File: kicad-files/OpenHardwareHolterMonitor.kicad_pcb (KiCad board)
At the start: 8 copper layers, 131 x 80 mm, 147 parts, among them CON1 Micro_SD_Card, J1 Conn_02x06_Odd_Even, J10 Conn_01x01, J11 Conn_01x01, J12 USB_OTG, J13 USB_C_Receptacle, J2 Conn_01x01, J3 Conn_01x01, J4 Conn_01x01, J5 Conn_01x01, J6 Conn_01x01, J7 Conn_01x01, J8 Conn_01x01, J9 Conn_01x01, P1 Custom_FTDI, Q1 S8050, Q10 Q_PMOS_DGS, Q2 S8050, Q3 Q_NMOS_DGS, Q4 Q_NMOS_DGS, Q5 Q_NMOS_DGS, Q6 Q_NMOS_DGS, Q7 Q_PMOS_DGS, Q8 Q_PMOS_DGS, Q9 Q_PMOS_DGS, SW1 SW_SPDT, U1 ESP-WROOM-32, U2 ADS1298, U3 MCP73833, U4 MCP73833, U5 TPS2113A, U6 LP5912, U7 REM_3-xxxxS, Y1 32768Hz

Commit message: checkpoint for kicad upgrade
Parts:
- added MH_NE: MountingHole_2.2mm_M2_ISO7380, Mounting_Holes:MountingHole_2.2mm_M2_ISO7380, F.Cu at (258.0, 28.0)
- added MH_NW: MountingHole_2.2mm_M2_ISO7380, Mounting_Holes:MountingHole_2.2mm_M2_ISO7380, F.Cu at (145.5, 43.5)
- added MH_SE: MountingHole_2.2mm_M2_ISO7380, Mounting_Holes:MountingHole_2.2mm_M2_ISO7380, F.Cu at (258.0, 92.0)
- added MH_SW: MountingHole_2.2mm_M2_ISO7380, Mounting_Holes:MountingHole_2.2mm_M2_ISO7380, F.Cu at (161.5, 84.0)
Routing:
- net /IO0: track 49.0 -> 46.0 mm
- net /EN: track 52.0 -> 51.3 mm
- net /RTS: track 33.9 -> 33.1 mm
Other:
- board text added: "EU: N (black)"
- board text added: "US: RL (green)"

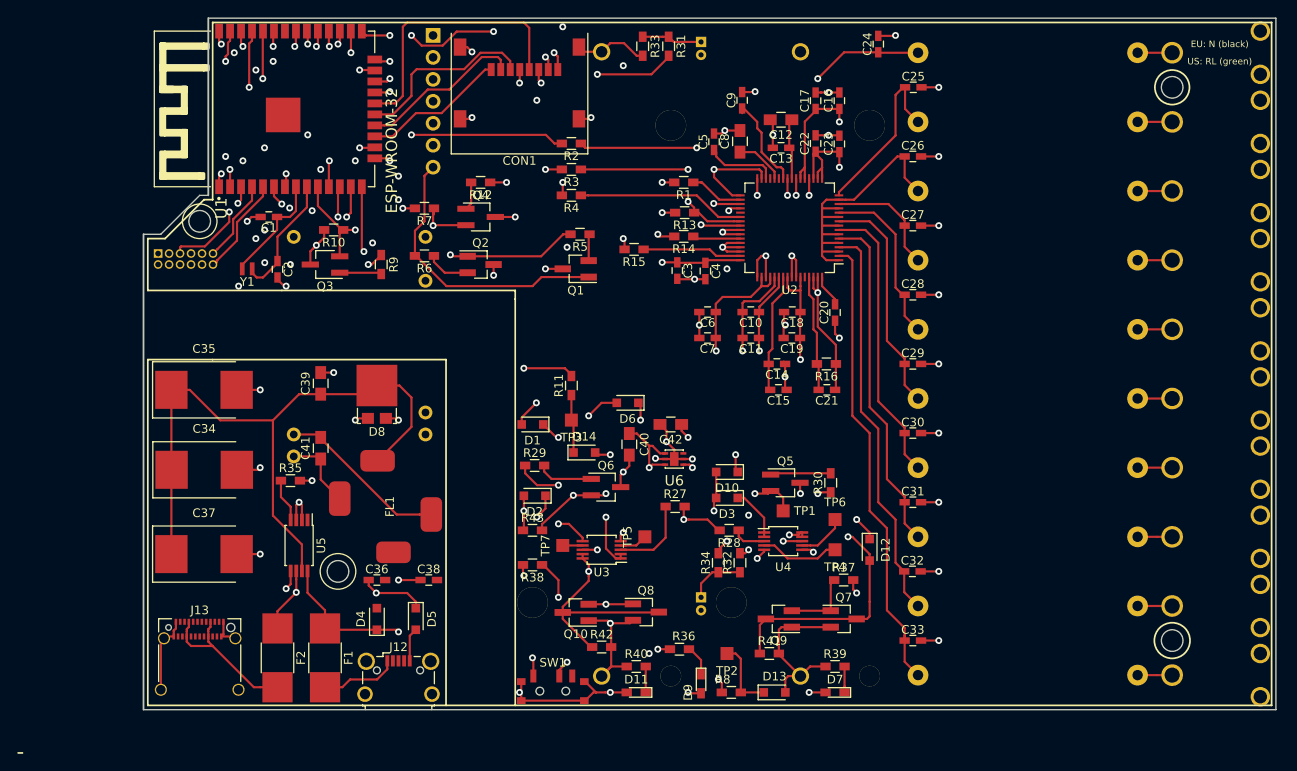
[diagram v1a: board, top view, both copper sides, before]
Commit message: switch to 6 layer board
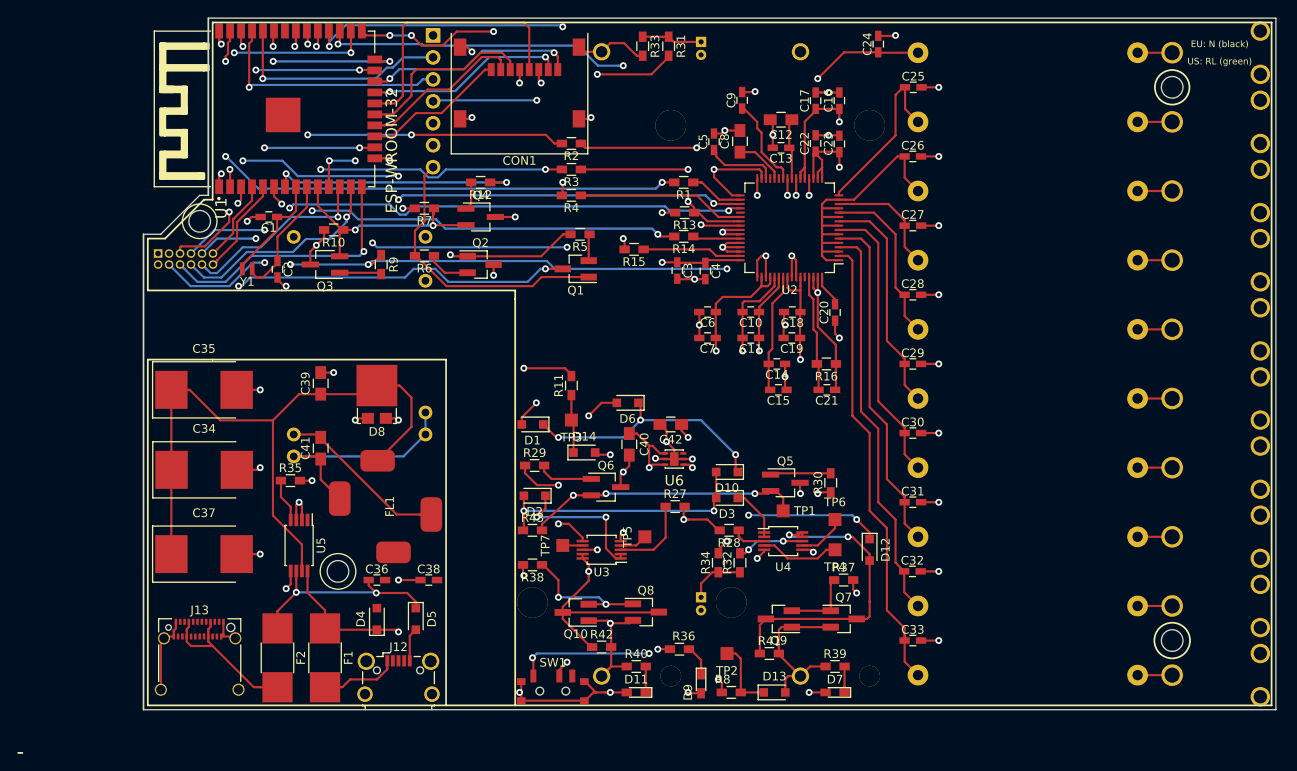
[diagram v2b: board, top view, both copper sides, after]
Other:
- copper layers 8 -> 6

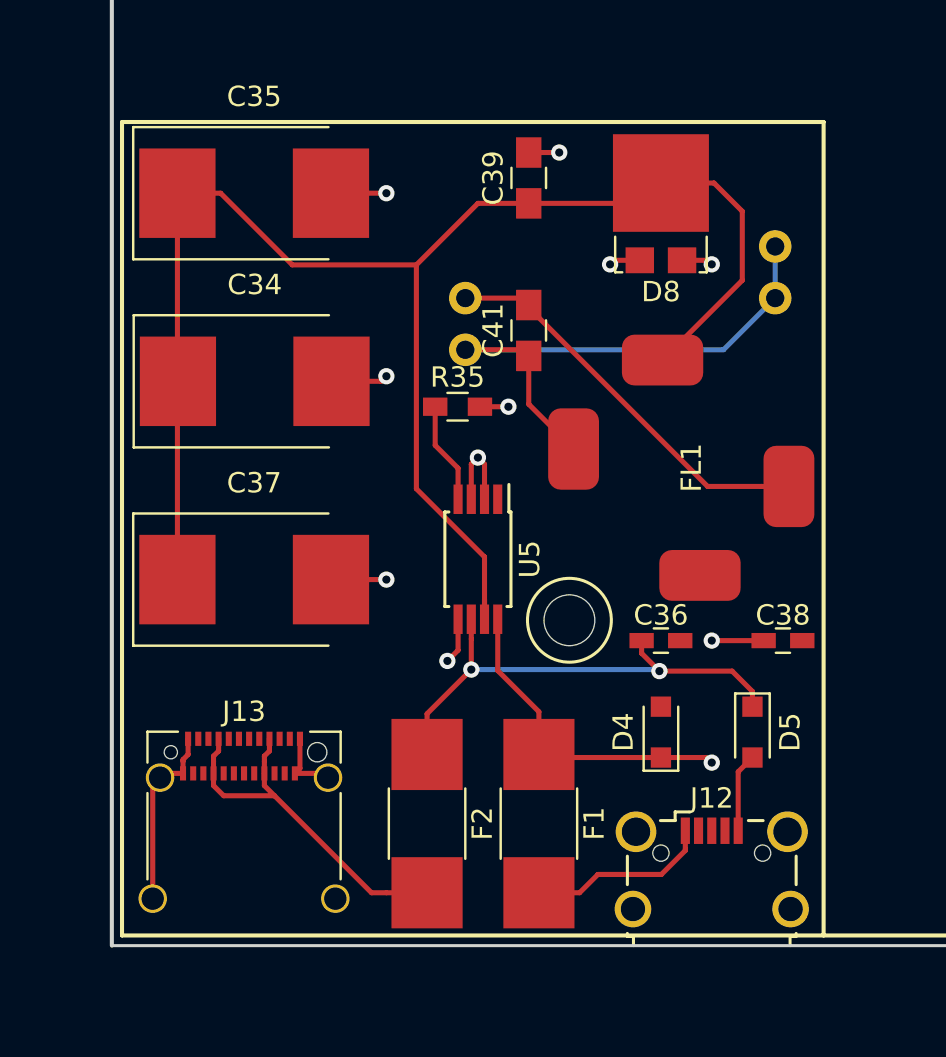
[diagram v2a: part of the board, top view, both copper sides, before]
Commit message: power lines 0.5mm
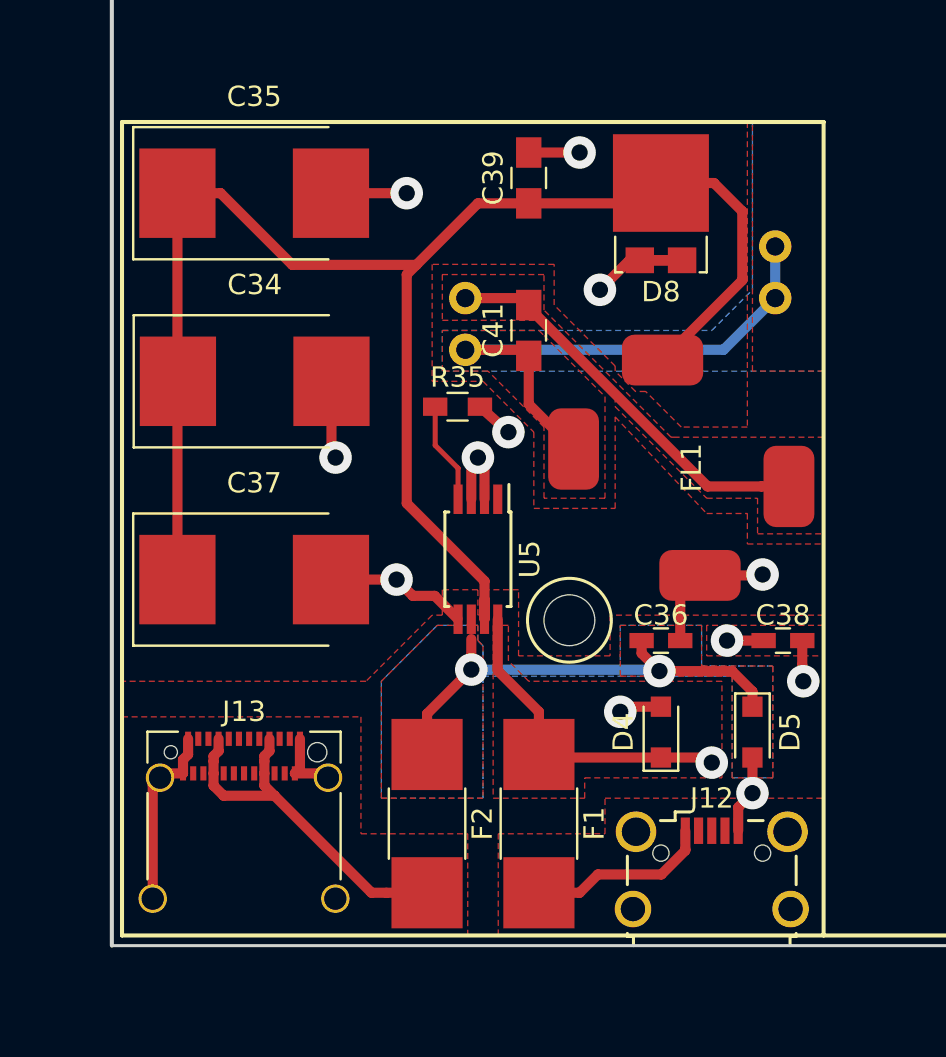
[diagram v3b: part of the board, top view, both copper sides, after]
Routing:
- net GNDPWR: track 37.4 -> 57.4 mm, vias 9 -> 11
- net /power/USB_C_IN: track 24.4 -> 23.5 mm
- added copper zone on In2.Cu.power, net (none)
- added copper zone on F.Cu, net +5C
- added copper zone on In2.Cu.power, net +5C
- added copper zone on F.Cu, net +5V
- added copper zone on F.Cu, net /power/MUX_POWER_OUT
- added copper zone on In2.Cu.power, net /power/MUX_POWER_OUT
- added copper zone on B.Cu, net /power/USB_C_IN
- added copper zone on F.Cu, net /power/USB_C_IN
- added copper zone on F.Cu, net /power/USB_MICRO_IN
- added copper zone on In3.Cu.vert, net /power/USB_MICRO_IN
- added copper zone on In1.Cu.gnd, net GNDPWR
- added copper zone on In4.Cu.gnd, net GNDPWR
- added copper zone on B.Cu, net Net-(C41-Pad1)
- added copper zone on F.Cu, net Net-(C41-Pad1)
- added copper zone on F.Cu, net Net-(C41-Pad2)
- added copper zone on In2.Cu.power, net Net-(C41-Pad2)
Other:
- net class Power added: clearance 0.2, trace_width 0.5, via_dia 1.6, via_drill 0.8

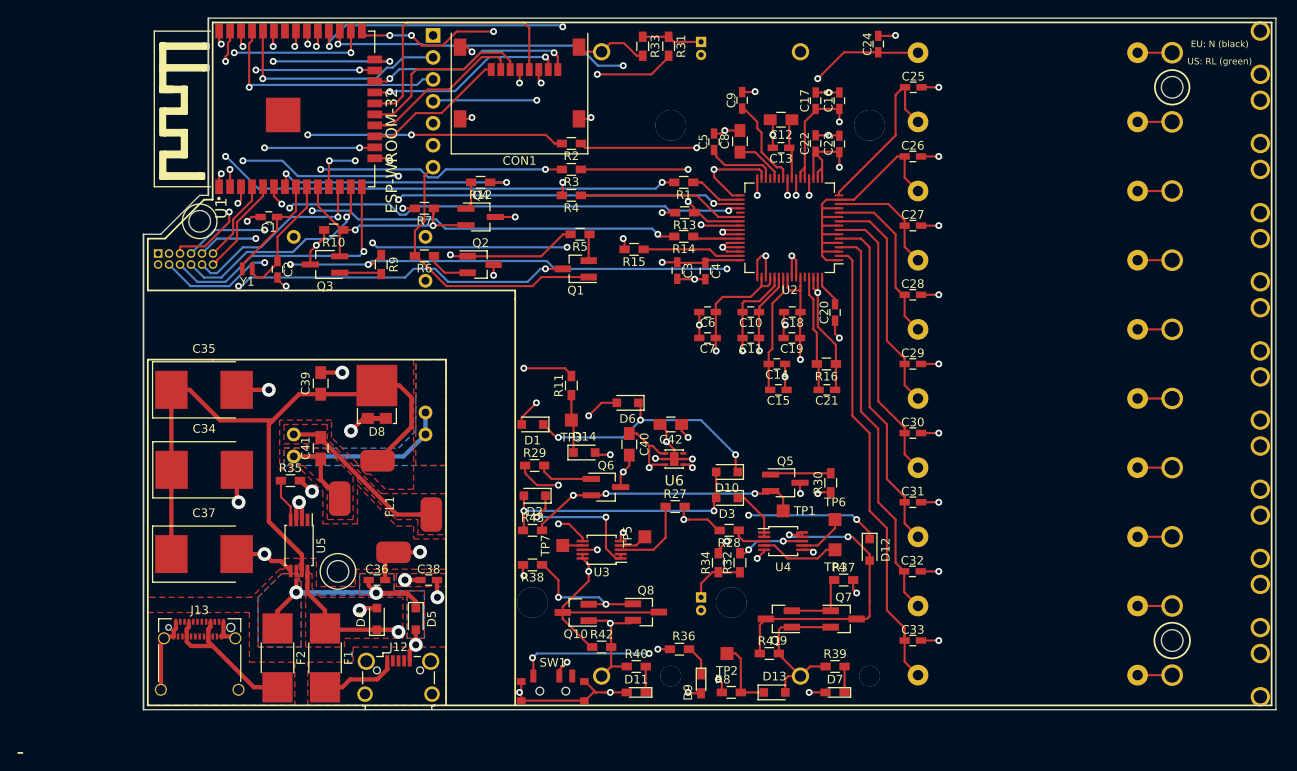
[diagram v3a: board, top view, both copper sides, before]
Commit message: isolated ground planes
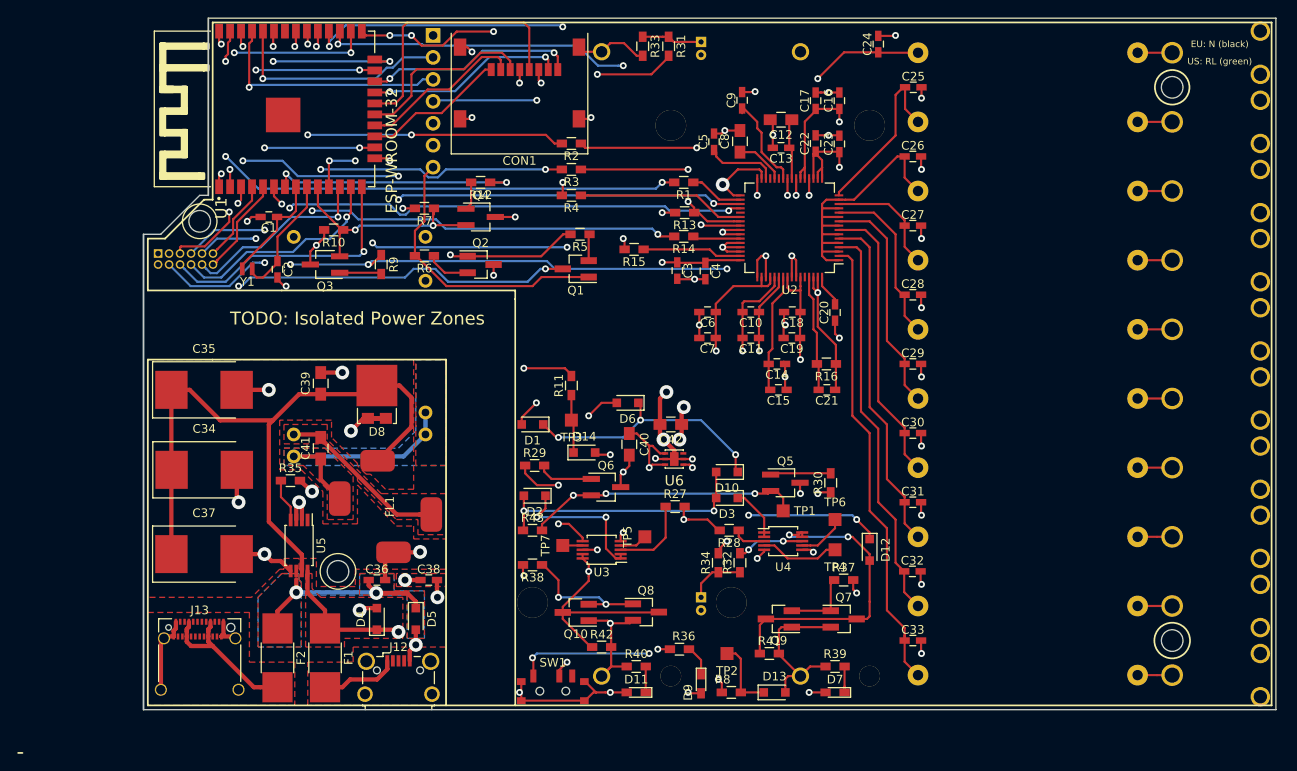
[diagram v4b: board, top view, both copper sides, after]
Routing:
- net GND: track 174.0 -> 170.5 mm, vias 56 -> 57
- net +3V3: track 109.3 -> 112.2 mm, vias 13 -> 14
- added copper zone on In2.Cu.power, net +3V3
- added copper zone on In1.Cu.gnd, net GND
- added copper zone on In4.Cu.gnd, net GND
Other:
- board text added: "TODO: Isolated Power Zones"

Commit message: widen power tracks
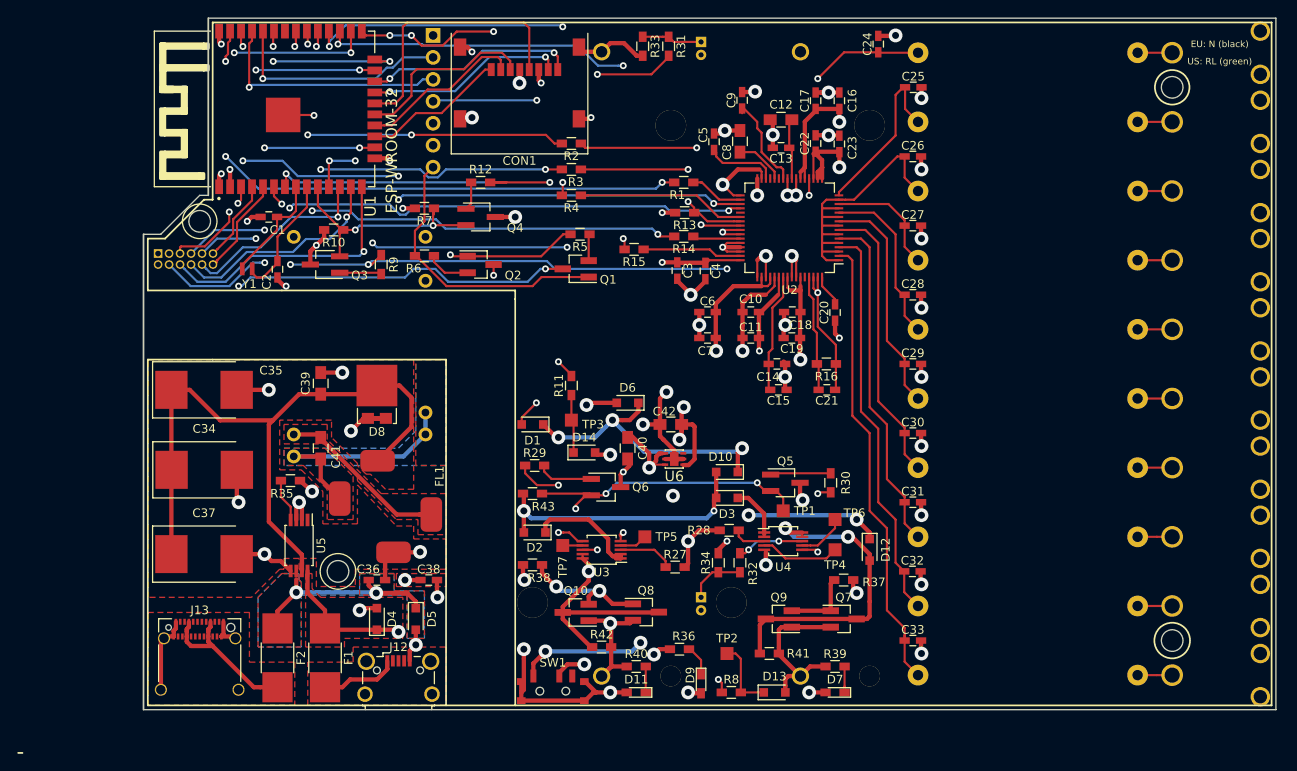
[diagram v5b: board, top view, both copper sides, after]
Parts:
- moved R27 7.00 mm to (200.5, 83.5)
- moved D2 4.25 mm to (184.2, 79.5)
- moved R43 4.25 mm to (184.0, 75.0)
- moved C40 0.49 mm to (195.0, 69.8)
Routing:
- net GND: track 170.5 -> 180.7 mm, vias 57 -> 56
- net /power/REGULATOR_IN: track 81.2 -> 88.3 mm
- net +3V3: track 112.2 -> 116.5 mm, vias 14 -> 13
- net Net-(D2-Pad1): track 17.2 -> 13.6 mm, vias 2 -> 0
- net (no net): track 0.00 -> 3.59 mm, vias 0 -> 1
- net /Bat2Charging: track 9.38 -> 6.44 mm
- net /Enable_Charging: track 100.6 -> 103.2 mm
- net /read_bat_2: track 57.7 -> 59.7 mm
- net Net-(C40-Pad1): track 47.2 -> 45.7 mm
- net Net-(D12-Pad2): track 35.9 -> 37.3 mm
- net Net-(D6-Pad2): track 46.8 -> 47.9 mm
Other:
- board text removed: "TODO: Isolated Power Zones"

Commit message: finishing up zones
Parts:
- U1: footprint ESP-WROOM-32:MODULE_ESP-WROOM-32 -> ESP-WROOM-32:MODULE_ESP-WROOM-32_NO_SILK_ANTENNA
- moved D1 10.4 mm to (185.5, 56.8), turned to 90 degrees
- moved R36 2.69 mm to (203.5, 92.0), turned to 90 degrees
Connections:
- U1 pad 1.1: (no net) -> GND
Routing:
- net GND: track 180.7 -> 211.8 mm, vias 56 -> 54
- net /FTDI_V: track 50.3 -> 37.3 mm
- net /power/REGULATOR_IN: track 88.3 -> 96.3 mm
- net +3V3: track 116.5 -> 121.8 mm
- net /power/MUX_POWER_OUT: track 79.6 -> 84.3 mm, vias 0 -> 2
- net (no net): track 3.59 -> 0.00 mm, vias 1 -> 0
- net /TXD0: track 28.3 -> 30.8 mm
- net /MOSI: track 68.5 -> 66.7 mm
- net /IO4: track 43.8 -> 42.1 mm
- net /Enable_Charging: track 103.2 -> 101.6 mm
- net /~CS~: track 44.9 -> 43.3 mm
- net /~PWDN~_OUT: track 76.7 -> 75.5 mm
- net Net-(D9-Pad1): track 3.57 -> 2.80 mm
- net /RXD0: track 26.2 -> 26.8 mm
- net /read_bat_1: track 112.9 -> 113.4 mm, vias 5 -> 7
- added copper zone on F.Cu, net +3V3
- added copper zone on In2.Cu.power, net /power/REGULATOR_IN
- added copper zone on B.Cu, net /power/V_ISO
- added copper zone on F.Cu, net /power/V_ISO
- added copper zone on In2.Cu.power, net /power/V_ISO
- added copper zone on B.Cu, net GND
- added copper zone on F.Cu, net GND
- added copper zone on B.Cu, net GNDPWR
- added copper zone on F.Cu, net Net-(BT1-Pad1)
- added copper zone on F.Cu, net Net-(BT2-Pad1)
- added copper zone on F.Cu, net Net-(D2-Pad1)
- added copper zone on F.Cu, net Net-(D3-Pad1)
